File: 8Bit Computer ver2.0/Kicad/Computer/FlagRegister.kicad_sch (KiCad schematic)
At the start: 9 parts, among them IC14 SN74HCS4075DR, IC15 SN74HCS32DR, IC16 SN74ABT821ADWR, IC42 SN74HCS08DR, IC43 SN74HCS74DR, IC46 SN74LVC1G14DBVR, IC47 SN74HCS08DR, IC48 SN74HCS74DR, IC49 SN74HCS74DR

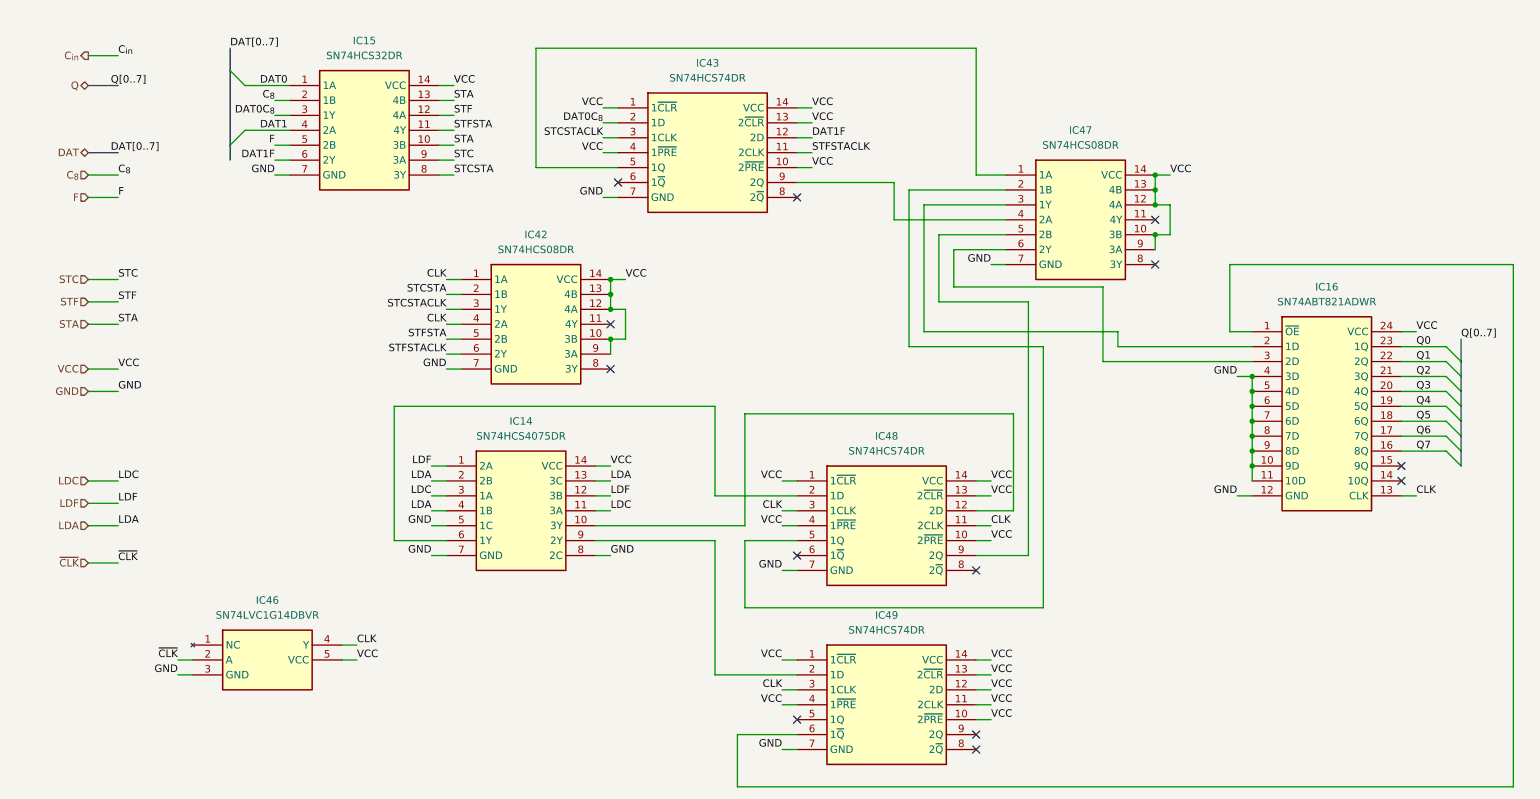
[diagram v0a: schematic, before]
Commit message: parts,Kicad
parts:
changed 8xDlatch HCS to ABT 574
waiting for SRAM CAD Model
Kicad:
imported AHC types of ICs
added ProgrammeCounter
finished Comparator
changed all HCS to AHC except 3in OR ->no AHC Version
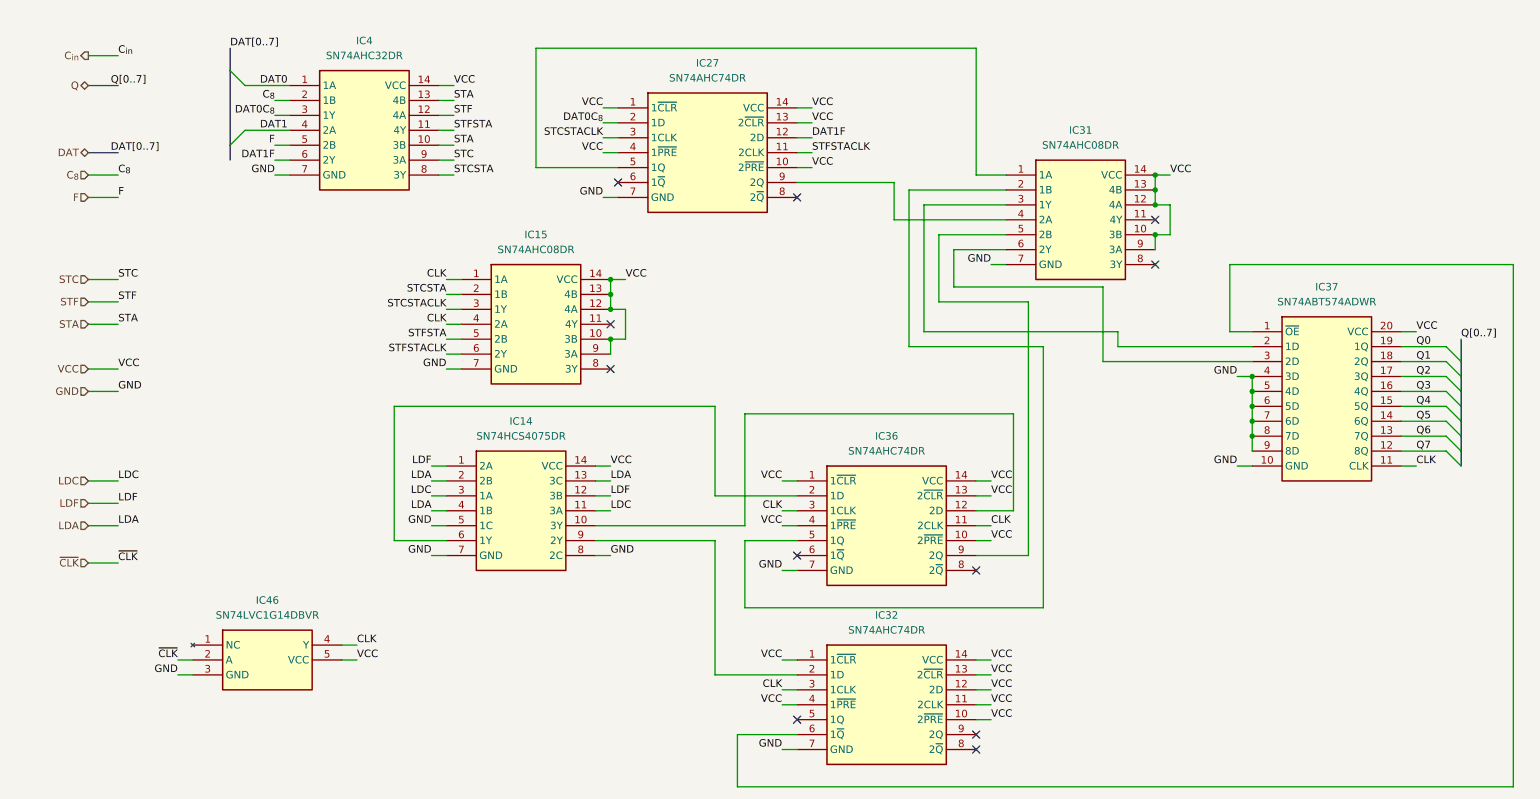
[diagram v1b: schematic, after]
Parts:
- removed IC15: SN74HCS32DR, Samacsys:SOIC127P600X175-14N, symbol Samacsys:SN74HCS32DR
- removed IC16: SN74ABT821ADWR, Samacsys:SOIC127P1030X265-24N, symbol Samacsys:SN74ABT821ADWR
- removed IC42, IC47: SN74HCS08DR, Samacsys:SOIC127P600X175-14N, symbol Samacsys:SN74HCS08DR
- removed IC43, IC48, IC49: SN74HCS74DR, Samacsys:SOIC127P600X175-14N, symbol Samacsys:SN74HCS74DR
- added IC15, IC31: SN74AHC08DR, Samacsys:SOIC127P600X175-14N, symbol Samacsys:SN74AHC08DR
- added IC27, IC32, IC36: SN74AHC74DR, Samacsys:SOIC127P600X175-14N, symbol Samacsys:SN74AHC74DR
- added IC37: SN74ABT574ADWR, Samacsys:SOIC127P1030X265-20N, symbol Samacsys:SN74ABT574ADWR
- added IC4: SN74AHC32DR, Samacsys:SOIC127P600X175-14N, symbol Samacsys:SN74AHC32DR
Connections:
- net CLK: now also IC15.1 (1A), IC15.4 (2A), IC32.3 (1CLK), IC36.11 (2CLK), IC36.3 (1CLK), IC37.11 (CLK)
- net C_{8}: now also IC4.2 (1B)
- net DAT0: now also IC4.1 (1A)
- net DAT0C_{8}: now also IC27.2 (1D), IC4.3 (1Y)
- net DAT1: now also IC4.4 (2A)
- net DAT1F: now also IC27.12 (2D), IC4.6 (2Y)
- net F: now also IC4.5 (2B)
- net GND: now also IC15.7 (GND), IC27.7 (GND), IC31.7 (GND), IC32.7 (GND), IC36.7 (GND), IC37.10 (GND), IC37.4 (3D), IC37.5 (4D), IC37.6 (5D), IC37.7 (6D), IC37.8 (7D), IC37.9 (8D), IC4.7 (GND)
- net Q0: now also IC37.19 (1Q)
- net Q1: now also IC37.18 (2Q)
- net Q2: now also IC37.17 (3Q)
- net Q3: now also IC37.16 (4Q)
- net Q4: now also IC37.15 (5Q)
- net Q5: now also IC37.14 (6Q)
- net Q6: now also IC37.13 (7Q)
- net Q7: now also IC37.12 (8Q)
- net STA: now also IC4.10 (3B), IC4.13 (4B)
- net STC: now also IC4.9 (3A)
- net STCSTA: now also IC15.2 (1B), IC4.8 (3Y)
- net STCSTACLK: now also IC15.3 (1Y), IC27.3 (1CLK)
- net STF: now also IC4.12 (4A)
- net STFSTA: now also IC15.5 (2B), IC4.11 (4Y)
- net STFSTACLK: now also IC15.6 (2Y), IC27.11 (2CLK)
- net VCC: now also IC15.10 (3B), IC15.12 (4A), IC15.13 (4B), IC15.14 (VCC), IC15.9 (3A), IC27.1 (1~{CLR}), IC27.10 (2~{PRE}), IC27.13 (2~{CLR}), IC27.14 (VCC), IC27.4 (1~{PRE}), IC31.10 (3B), IC31.12 (4A), IC31.13 (4B), IC31.14 (VCC), IC31.9 (3A), IC32.1 (1~{CLR}), IC32.10 (2~{PRE}), IC32.11 (2CLK), IC32.12 (2D), IC32.13 (2~{CLR}), IC32.14 (VCC), IC32.4 (1~{PRE}), IC36.1 (1~{CLR}), IC36.10 (2~{PRE}), IC36.13 (2~{CLR}), IC36.14 (VCC), IC36.4 (1~{PRE}), IC37.20 (VCC), IC4.14 (VCC)
- net at IC14.10 (3Y): now also IC36.12 (2D)
- net at IC14.6 (1Y): now also IC36.2 (1D)
- net at IC14.9 (2Y): now also IC32.2 (1D)
- new net: IC27.5 (1Q), IC31.1 (1A)
- new net: IC27.9 (2Q), IC31.4 (2A)
- new net: IC32.6 (1~{Q}), IC37.1 (~{OE})
- new net: IC31.3 (1Y), IC37.2 (1D)
- new net: IC31.6 (2Y), IC37.3 (2D)
- new net: IC31.2 (1B), IC36.5 (1Q)
- new net: IC31.5 (2B), IC36.9 (2Q)
- no-connect marks 13 -> 11

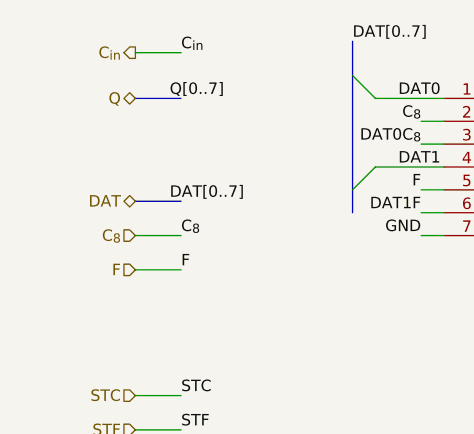
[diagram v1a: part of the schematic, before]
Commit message: Kicad
added Register 2(0x22 u 0x23) and 3(0x13 u 0x14)
added BarrelShiftRegister
added AdderSubstractor
added cmd Comparators to the bitwise and binary Logic
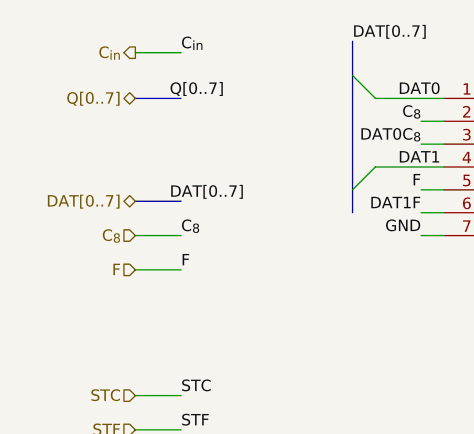
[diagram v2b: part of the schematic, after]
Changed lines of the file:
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@@
 		)
 	)
-	(hierarchical_label "DAT"
+	(hierarchical_label "DAT[0..7]"
 		(shape tri_state)
 		(at 31.75 43.18 180)
@@
 		)
 	)
-	(hierarchical_label "Q"
+	(hierarchical_label "Q[0..7]"
 		(shape tri_state)
 		(at 31.75 31.75 180)

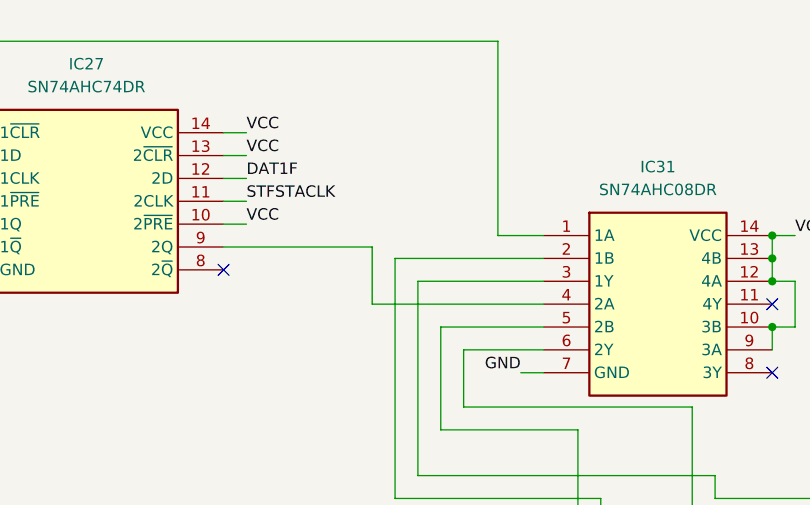
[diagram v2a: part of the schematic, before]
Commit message: Kicad
included Delay, pin Strips and headers, 8xnot
added some comps
finished flash mem
added DATtoADR
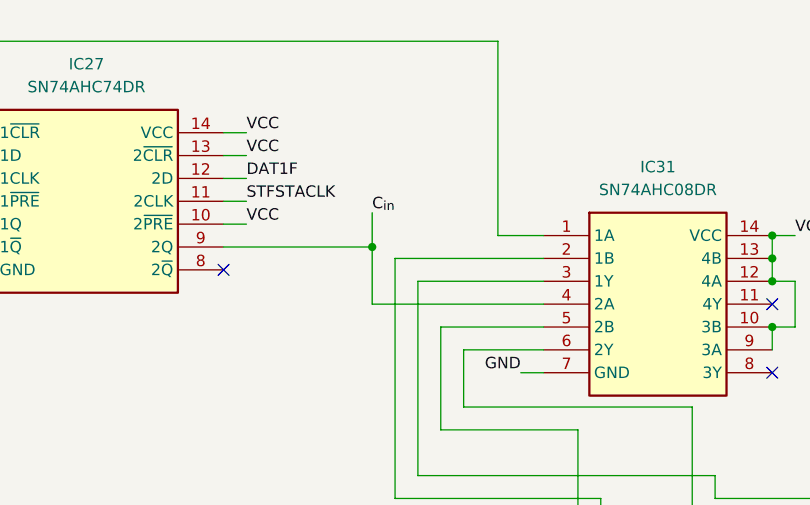
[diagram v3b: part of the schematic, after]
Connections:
- net C_{in}: now also IC27.9 (2Q), IC31.4 (2A)
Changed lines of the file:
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@@
+	)
+	(junction
+		(at 168.91 48.26)
+		(diameter 0)
+		(color 0 0 0 0)
 	)
 	(junction
@@
 	(wire
 		(pts
+			(xy 168.91 44.45) (xy 168.91 48.26)
+		)
+		(stroke
+			(width 0)
+			(type default)
+		)
+	)
+	(wire
+		(pts
 			(xy 92.71 64.77) (xy 95.25 64.77)
 		)
@@
 		(effects
 			(font
+				(size 1.27 1.27)
+			)
+			(justify left bottom)
+		)
+	)
+	(label "C_{in}"
+		(at 168.91 44.45 0)
+		(effects
+			(font

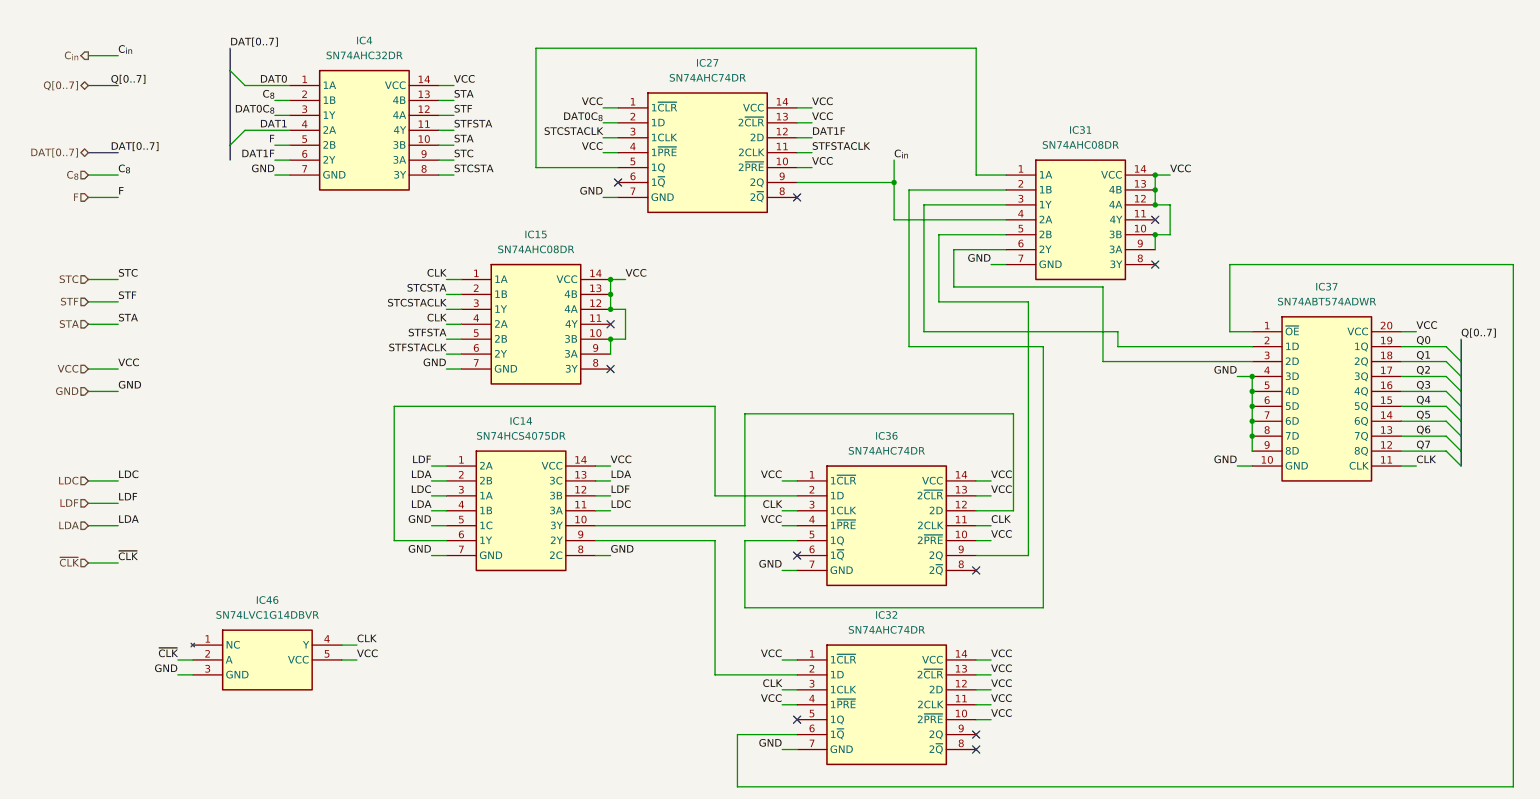
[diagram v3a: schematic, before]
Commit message: Kicad, parts
Parts:
added Leds
Kicad:
added Input Output
changed Q bus to DAT bus
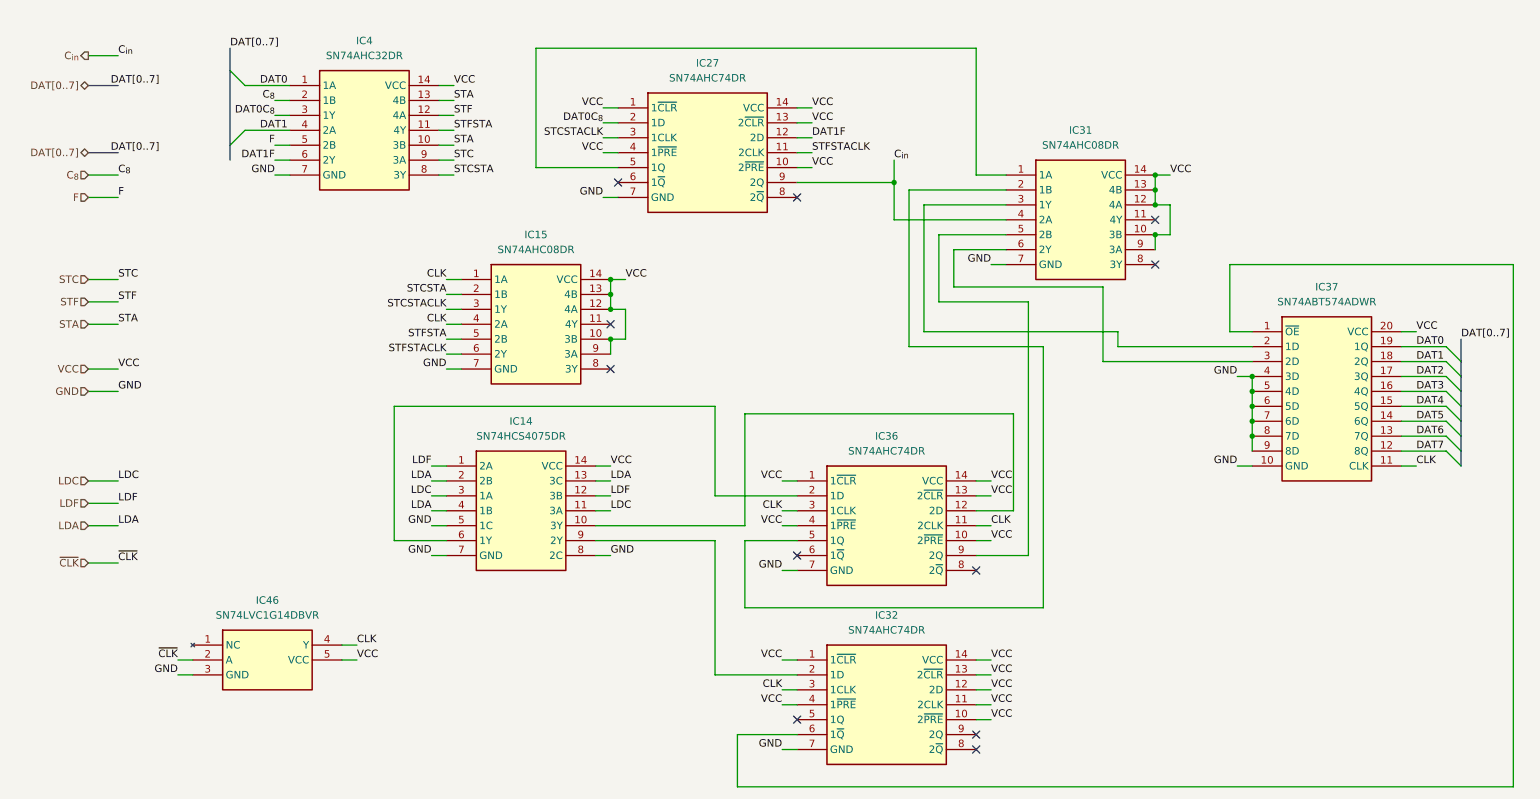
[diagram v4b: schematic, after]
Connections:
- net Q0 is gone; now on net DAT0: IC37.19 (1Q)
- net Q1 is gone; now on net DAT1: IC37.18 (2Q)
- net Q2 renamed DAT2
- net Q3 renamed DAT3
- net Q4 renamed DAT4
- net Q5 renamed DAT5
- net Q6 renamed DAT6
- net Q7 renamed DAT7
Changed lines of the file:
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@@
 		)
 	)
-	(label "Q6"
+	(label "DAT6"
 		(at 257.81 91.44 0)
 		(effects
@@
 		)
 	)
-	(label "Q3"
+	(label "DAT3"
 		(at 257.81 83.82 0)
 		(effects
@@
 		)
 	)
-	(label "Q1"
+	(label "DAT1"
 		(at 257.81 78.74 0)
 		(effects
@@
 		)
 	)
-	(label "Q5"
+	(label "DAT5"
 		(at 257.81 88.9 0)
 		(effects
@@
 		)
 	)
-	(label "Q7"
+	(label "DAT7"
 		(at 257.81 93.98 0)
 		(effects
@@
 		)
 	)
-	(label "Q[0..7]"
+	(label "DAT[0..7]"
 		(at 265.43 74.93 0)
 		(effects
@@
 		)
 	)
-	(label "Q2"
+	(label "DAT2"
 		(at 257.81 81.28 0)
 		(effects
@@
 		)
 	)
-	(label "Q0"
+	(label "DAT0"
 		(at 257.81 76.2 0)
 		(effects
@@
 		)
 	)
-	(label "Q[0..7]"
+	(label "DAT[0..7]"
 		(at 35.56 31.75 0)
 		(effects
@@
 		)
 	)
-	(label "Q4"
+	(label "DAT4"
 		(at 257.81 86.36 0)
 		(effects
@@
 		)
 	)
-	(hierarchical_label "Q[0..7]"
+	(hierarchical_label "DAT[0..7]"
 		(shape tri_state)
 		(at 31.75 31.75 180)

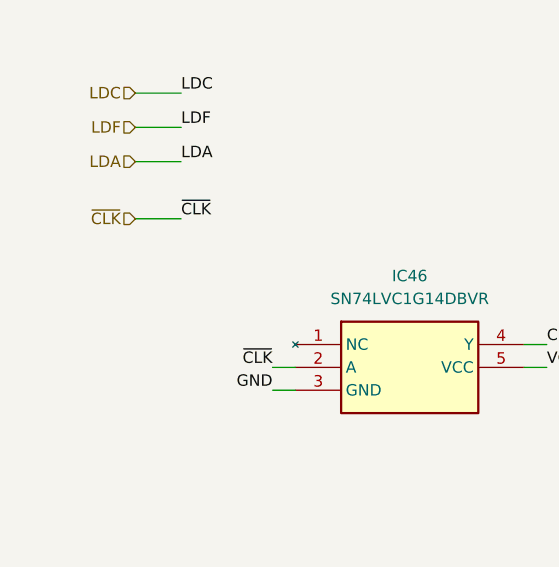
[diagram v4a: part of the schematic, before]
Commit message: Kicad, parts
parts:
added USB C PD Triggerboard
added Delay Chip for 90ns
added Push Button
Kicad:
added USB C PD Triggerboard
added rising edge detector via Delay and Xor for Accept Push Button
added VBUS net
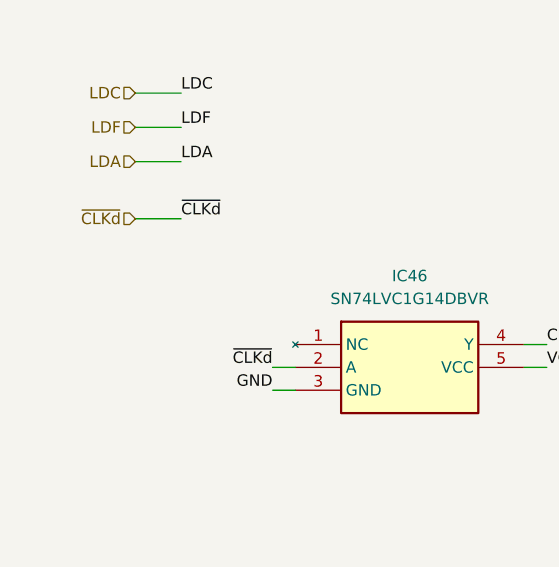
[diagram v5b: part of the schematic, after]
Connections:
- net ~{CLK} renamed ~{CLKd}
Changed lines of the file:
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@@
 		)
 	)
-	(label "~{CLK}"
+	(label "~{CLKd}"
 		(at 46.99 129.54 180)
 		(effects
@@
 		)
 	)
-	(label "~{CLK}"
+	(label "~{CLKd}"
 		(at 36.83 113.03 0)
 		(effects
@@
 		)
 	)
-	(hierarchical_label "~{CLK}"
+	(hierarchical_label "~{CLKd}"
 		(shape input)
 		(at 31.75 113.03 180)
